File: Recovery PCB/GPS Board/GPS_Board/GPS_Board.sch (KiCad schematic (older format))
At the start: 10 parts, among them J1 XT30-M, J2 XT30-M, U1 Teensy4.1

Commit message: Added regulator symbols
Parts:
- removed A3: Eboot-MP1584EN-5V-Power-Supply, GPS Board:EBOOT-MP1584EN-5N-POWER-SUPPLY, symbol eboot-mp1584en-5v-power-supply:Eboot-MP1584EN-5V-Power-Supply
- added U?: D24V22F5_VoltageRegulator, symbol GPS_Board:D24V22F5_VoltageRegulator
- added U?: LD1117v33, symbol GPS_Board:LD1117v33
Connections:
- wire segments 52 -> 53
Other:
- moved on the sheet: J1, J2
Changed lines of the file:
@@
-$EndComp
-$Comp
-L eboot-mp1584en-5v-power-supply:Eboot-MP1584EN-5V-Power-Supply A3
-U 1 1 61A8FD6D
-P 9400 1950
-F 0 "A3" H 9400 2615 50  0000 C CNN
-F 1 "Eboot-MP1584EN-5V-Power-Supply" H 9400 2524 50  0000 C CNN
-F 2 "GPS Board:EBOOT-MP1584EN-5N-POWER-SUPPLY" H 9400 1950 50  0001 C CNN
-F 3 "" H 9400 1950 50  0001 C CNN
-	1    9400 1950
-	1    0    0    -1
 $EndComp
 $Comp
 L GPS_Board:XT30-M J1
 U 1 1 61A95F1A
-P 7250 2000
-F 0 "J1" V 7216 2468 50  0000 L CNN
-F 1 "XT30-M" V 7307 2468 50  0000 L CNN
-F 2 "Connector_AMASS:AMASS_XT30U-M_1x02_P5.0mm_Vertical" H 7250 2000 50  0001 C CNN
-F 3 "" H 7250 2000 50  0001 C CNN
-	1    7250 2000
+P 7225 1400
+F 0 "J1" V 7191 1868 50  0000 L CNN
+F 1 "XT30-M" V 7282 1868 50  0000 L CNN
+F 2 "Connector_AMASS:AMASS_XT30U-M_1x02_P5.0mm_Vertical" H 7225 1400 50  0001 C CNN
+F 3 "" H 7225 1400 50  0001 C CNN
+	1    7225 1400
 	0    1    1    0
 $EndComp
@@
 L GPS_Board:XT30-M J2
 U 1 1 61A98361
-P 8100 2300
-F 0 "J2" H 7923 2466 50  0000 R CNN
-F 1 "XT30-M" H 7923 2557 50  0000 R CNN
-F 2 "Connector_AMASS:AMASS_XT30U-M_1x02_P5.0mm_Vertical" H 8100 2300 50  0001 C CNN
-F 3 "" H 8100 2300 50  0001 C CNN
-	1    8100 2300
+P 8075 1700
+F 0 "J2" H 7898 1866 50  0000 R CNN
+F 1 "XT30-M" H 7898 1957 50  0000 R CNN
+F 2 "Connector_AMASS:AMASS_XT30U-M_1x02_P5.0mm_Vertical" H 8075 1700 50  0001 C CNN
+F 3 "" H 8075 1700 50  0001 C CNN
+	1    8075 1700
 	-1   0    0    1
 $EndComp
 Wire Wire Line
-	7250 2100 7100 2100
-Wire Wire Line
-	7100 2100 7100 2250
-Wire Wire Line
-	7100 2250 8000 2250
-Wire Wire Line
-	8000 2250 8000 2300
-Wire Wire Line
-	8175 2300 8175 2250
-Wire Wire Line
-	8175 2250 8600 2250
-Wire Wire Line
-	8600 2250 8600 2400
-Wire Wire Line
-	8600 1550 7075 1550
-Wire Wire Line
-	7075 1550 7075 1925
-Wire Wire Line
-	7075 1925 7250 1925
+	7225 1500 7075 1500
+Wire Wire Line
+	7075 1500 7075 1650
+Wire Wire Line
+	7075 1650 7975 1650
+Wire Wire Line
+	7975 1650 7975 1700
+Wire Wire Line
+	8150 1700 8150 1650
+Wire Wire Line
+	8150 1650 8575 1650
+Wire Wire Line
+	8575 1650 8575 1800
+Wire Wire Line
+	6975 1325 7225 1325
 $Comp
 L GPS_Board:Sparkfun-GPS-Breakout A2
@@
 F 3 "" H 4000 1500 50  0001 C CNN
 	1    4000 1500
-	0    -1   -1   0
-$EndComp
-$Comp
-L power:GND #PWR0104
-U 1 1 61AC16D1
-P 10200 1550
-F 0 "#PWR0104" H 10200 1300 50  0001 C CNN
-F 1 "GND" V 10205 1422 50  0000 R CNN
-F 2 "" H 10200 1550 50  0001 C CNN
-F 3 "" H 10200 1550 50  0001 C CNN
-	1    10200 1550
 	0    -1   -1   0
 $EndComp
@@
 	0    1    1    0
 $EndComp
-$Comp
-L power:+5V #PWR0108
-U 1 1 61AD2A6D
-P 10200 2400
-F 0 "#PWR0108" H 10200 2250 50  0001 C CNN
-F 1 "+5V" V 10215 2528 50  0000 L CNN
-F 2 "" H 10200 2400 50  0001 C CNN
-F 3 "" H 10200 2400 50  0001 C CNN
-	1    10200 2400
-	0    1    1    0
-$EndComp
 Wire Wire Line
 	2900 4850 2950 4850
@@
 	1    0    0    -1
 $EndComp
-$Comp
-L power:GND #PWR?
-U 1 1 61BA5EBA
-P 7075 1550
-F 0 "#PWR?" H 7075 1300 50  0001 C CNN
-F 1 "GND" H 7080 1377 50  0000 C CNN
-F 2 "" H 7075 1550 50  0001 C CNN
-F 3 "" H 7075 1550 50  0001 C CNN
-	1    7075 1550
-	-1   0    0    1
-$EndComp
-Connection ~ 7075 1550
 Wire Wire Line
 	4000 2200 4300 2200
@@
 Text Label 4400 3200 2    39   ~ 0
 XBee_DTR
-Text Label 6675 1925 2    39   ~ 0
-ON_SLEEP
 Wire Wire Line
 	4000 3700 4425 3700
@@
 Wire Wire Line
 	6275 1525 6575 1525
-Wire Wire Line
-	6275 1925 6675 1925
 Wire Wire Line
 	6275 2125 6675 2125
@@
 Text Label 4300 2400 2    39   ~ 0
 XBEE_SCL
+Wire Wire Line
+	6275 1925 6675 1925
+Text Label 6675 1925 2    39   ~ 0
+ON_SLEEP
+$Comp
+L GPS_Board:D24V22F5_VoltageRegulator U?
+U 1 1 6257FB96
+P 9300 1900
+F 0 "U?" H 9578 1946 50  0000 L CNN
+F 1 "D24V22F5_VoltageRegulator" H 9578 1855 50  0000 L CNN
+F 2 "" H 9750 3100 50  0001 C CNN
+F 3 "" H 9750 3100 50  0001 C CNN
+	1    9300 1900
+	1    0    0    -1
+$EndComp
+Wire Wire Line
+	8950 1800 8575 1800
+$Comp
+L power:GND #PWR?
+U 1 1 62587171
+P 6975 1325
+F 0 "#PWR?" H 6975 1075 50  0001 C CNN
+F 1 "GND" H 6980 1152 50  0000 C CNN
+F 2 "" H 6975 1325 50  0001 C CNN
+F 3 "" H 6975 1325 50  0001 C CNN
+	1    6975 1325
+	1    0    0    -1
+$EndComp
+$Comp
+L power:+5V #PWR?
+U 1 1 62588B60
+P 8950 2100
+F 0 "#PWR?" H 8950 1950 50  0001 C CNN
+F 1 "+5V" V 8965 2228 50  0000 L CNN
+F 2 "" H 8950 2100 50  0001 C CNN
+F 3 "" H 8950 2100 50  0001 C CNN
+	1    8950 2100
+	0    -1   -1   0
+$EndComp
+$Comp
+L power:GND #PWR?
+U 1 1 62589874
+P 8950 1900
+F 0 "#PWR?" H 8950 1650 50  0001 C CNN
+F 1 "GND" V 8955 1772 50  0000 R CNN
+F 2 "" H 8950 1900 50  0001 C CNN
+F 3 "" H 8950 1900 50  0001 C CNN
+	1    8950 1900
+	0    1    1    0
+$EndComp
+$Comp
+L power:GND #PWR?
+U 1 1 6258A3E2
+P 8950 2000
+F 0 "#PWR?" H 8950 1750 50  0001 C CNN
+F 1 "GND" V 8955 1872 50  0000 R CNN
+F 2 "" H 8950 2000 50  0001 C CNN
+F 3 "" H 8950 2000 50  0001 C CNN
+	1    8950 2000
+	0    1    1    0
+$EndComp
+$Comp
+L GPS_Board:LD1117v33 U?
+U 1 1 625AB452
+P 9300 2675
+F 0 "U?" H 9290 3020 50  0000 C CNN
+F 1 "LD1117v33" H 9290 2929 50  0000 C CNN
+F 2 "" H 9290 2905 50  0001 C CNN
+F 3 "" H 9290 2905 50  0001 C CNN
+	1    9300 2675
+	1    0    0    -1
+$EndComp
+Wire Wire Line
+	8575 2675 8575 1800
+Connection ~ 8575 1800
+Wire Wire Line
+	8575 2675 8940 2675
+$Comp
+L power:GND #PWR?
+U 1 1 625C6B48
+P 9640 2765
+F 0 "#PWR?" H 9640 2515 50  0001 C CNN
+F 1 "GND" V 9645 2637 50  0000 R CNN
+F 2 "" H 9640 2765 50  0001 C CNN
+F 3 "" H 9640 2765 50  0001 C CNN
+	1    9640 2765
+	0    -1   -1   0
+$EndComp
+$Comp
+L power:+3.3V #PWR?
+U 1 1 625C7E59
+P 9640 2605
+F 0 "#PWR?" H 9640 2455 50  0001 C CNN
+F 1 "+3.3V" V 9655 2733 50  0000 L CNN
+F 2 "" H 9640 2605 50  0001 C CNN
+F 3 "" H 9640 2605 50  0001 C CNN
+	1    9640 2605
+	0    1    1    0
+$EndComp
 $EndSCHEMATC

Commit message: Added footprint to 3.3v regulator
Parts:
- U?: footprint (none) -> GPS Board:D24V22F5_VoltageRegulator
- U?: footprint (none) -> Package_TO_SOT_THT:TO-220-3_Horizontal_TabDown
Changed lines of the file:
@@
 F 0 "U?" H 9578 1946 50  0000 L CNN
 F 1 "D24V22F5_VoltageRegulator" H 9578 1855 50  0000 L CNN
-F 2 "" H 9750 3100 50  0001 C CNN
+F 2 "GPS Board:D24V22F5_VoltageRegulator" H 9750 3100 50  0001 C CNN
 F 3 "" H 9750 3100 50  0001 C CNN
 	1    9300 1900
@@
 F 0 "U?" H 9290 3020 50  0000 C CNN
 F 1 "LD1117v33" H 9290 2929 50  0000 C CNN
-F 2 "" H 9290 2905 50  0001 C CNN
+F 2 "Package_TO_SOT_THT:TO-220-3_Horizontal_TabDown" H 9290 2905 50  0001 C CNN
 F 3 "" H 9290 2905 50  0001 C CNN
 	1    9300 2675

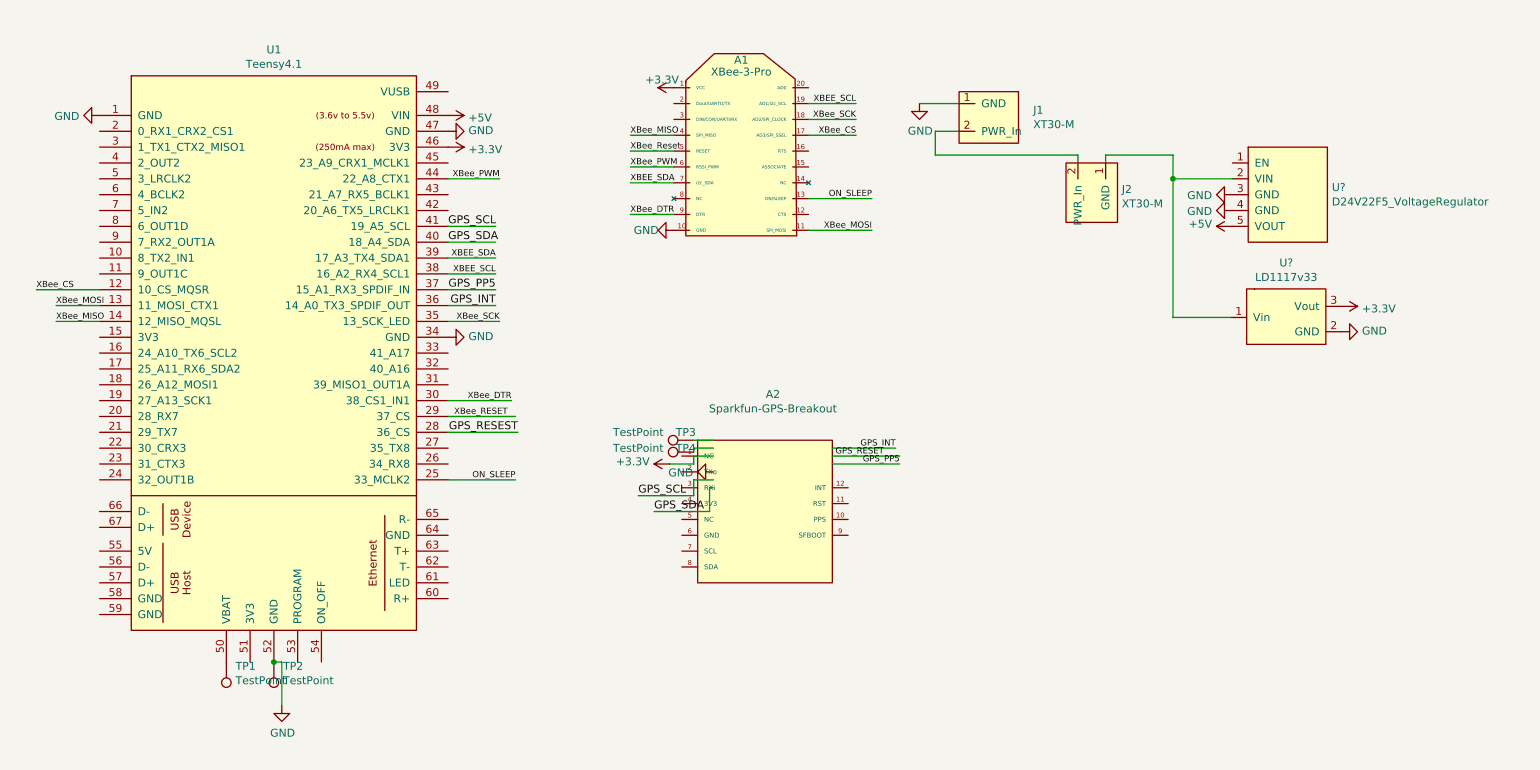
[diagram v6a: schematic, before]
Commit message: Added UART labels and testpoints
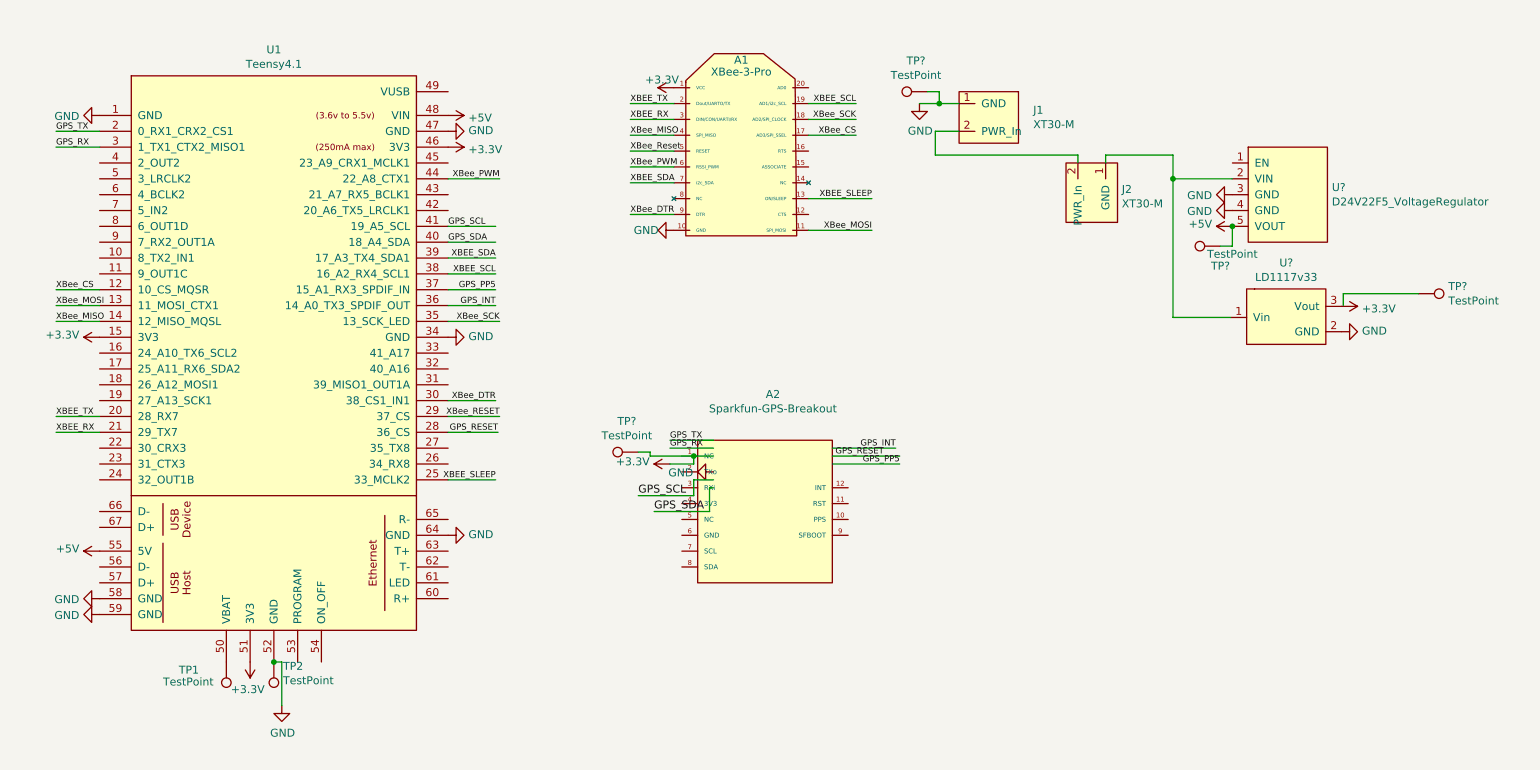
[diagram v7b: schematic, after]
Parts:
- removed TP3, TP4: TestPoint, TestPoint:TestPoint_Pad_D1.5mm, symbol Connector:TestPoint
- added TP? (x4): TestPoint, symbol Connector:TestPoint
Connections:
- net labels added: GPS_RX, GPS_TX, XBEE_RX, XBEE_SLEEP, XBEE_TX
- net labels removed: GPS_RESEST, ON_SLEEP
- wire segments 53 -> 68
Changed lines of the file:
@@
 	8575 1650 8575 1800
 Wire Wire Line
-	6975 1325 7225 1325
+	6975 1325 7100 1325
 $Comp
 L GPS_Board:Sparkfun-GPS-Breakout A2
@@
 	1    0    0    -1
 $EndComp
-$Comp
-L Connector:TestPoint TP3
-U 1 1 61AB8223
-P 5550 3450
-F 0 "TP3" V 5600 3500 50  0000 C CNN
-F 1 "TestPoint" V 5600 3800 50  0000 C CNN
-F 2 "TestPoint:TestPoint_Pad_D1.5mm" H 5750 3450 50  0001 C CNN
-F 3 "~" H 5750 3450 50  0001 C CNN
-	1    5550 3450
-	0    -1   -1   0
-$EndComp
-$Comp
-L Connector:TestPoint TP4
-U 1 1 61AB9396
-P 5550 3525
-F 0 "TP4" V 5575 3575 50  0000 C CNN
-F 1 "TestPoint" V 5575 3875 50  0000 C CNN
-F 2 "TestPoint:TestPoint_Pad_D1.5mm" H 5750 3525 50  0001 C CNN
-F 3 "~" H 5750 3525 50  0001 C CNN
-	1    5550 3525
-	0    -1   -1   0
-$EndComp
-Wire Wire Line
-	5550 3450 5675 3450
-Wire Wire Line
-	5550 3525 5550 3500
-Wire Wire Line
-	5550 3500 5675 3500
+Wire Wire Line
+	5400 3450 5675 3450
+Wire Wire Line
+	5400 3500 5675 3500
 $Comp
 L power:GND #PWR0101
@@
 U 1 1 61ACF9DD
 P 2600 4850
-F 0 "TP1" H 2542 4876 50  0000 R CNN
-F 1 "TestPoint" H 2542 4967 50  0000 R CNN
+F 0 "TP1" H 2900 4900 50  0000 R CNN
+F 1 "TestPoint" H 3000 4975 50  0000 R CNN
 F 2 "TestPoint:TestPoint_Pad_D1.5mm" H 2800 4850 50  0001 C CNN
 F 3 "~" H 2800 4850 50  0001 C CNN
@@
 Wire Wire Line
 	5650 3750 5675 3750
-Text Label 4000 2100 0    50   ~ 0
+Text Label 4000 2100 0    39   ~ 0
 GPS_SCL
-Text Label 4000 2200 0    50   ~ 0
+Text Label 4000 2200 0    39   ~ 0
 GPS_SDA
 Text Label 5200 3800 0    50   ~ 0
@@
 	0    -1   -1   0
 $EndComp
-Text Label 4440 3400 2    50   ~ 0
-GPS_RESEST
-Wire Wire Line
-	4000 3400 4440 3400
+Text Label 4315 3400 2    39   ~ 0
+GPS_RESET
+Wire Wire Line
+	4000 3400 4315 3400
 Text Label 6750 3550 2    39   ~ 0
 GPS_RESET
@@
 Wire Wire Line
 	6425 3600 6850 3600
-Text Label 4300 2500 2    50   ~ 0
+Text Label 4300 2500 2    39   ~ 0
 GPS_PP5
 Wire Wire Line
@@
 Wire Wire Line
 	4000 2600 4300 2600
-Text Label 4300 2600 2    50   ~ 0
+Text Label 4300 2600 2    39   ~ 0
 GPS_INT
 Text Label 6825 3500 2    39   ~ 0
@@
 Text Label 6575 1425 2    39   ~ 0
 XBee_SCK
-Text Label 1400 2500 0    39   ~ 0
+Text Label 1525 2500 0    39   ~ 0
 XBee_CS
 Wire Wire Line
-	1400 2500 1800 2500
+	1525 2500 1800 2500
 $Comp
 L power:+3.3V #PWR?
@@
 	1800 2700 1525 2700
 Wire Wire Line
-	4000 3300 4425 3300
-Text Label 4375 3300 2    39   ~ 0
+	4000 3300 4325 3300
+Text Label 4325 3300 2    39   ~ 0
 XBee_RESET
 Text Label 5150 1725 0    39   ~ 0
@@
 XBee_DTR
 Wire Wire Line
-	4000 3200 4400 3200
-Text Label 4400 3200 2    39   ~ 0
+	4000 3200 4300 3200
+Text Label 4300 3200 2    39   ~ 0
 XBee_DTR
 Wire Wire Line
-	4000 3700 4425 3700
-Text Label 4425 3700 2    39   ~ 0
-ON_SLEEP
+	4000 3700 4300 3700
+Text Label 4300 3700 2    39   ~ 0
+XBEE_SLEEP
 $Comp
 L power:+3.3V #PWR?
@@
 Text Label 6675 2125 2    39   ~ 0
 XBee_MOSI
-Wire Wire Line
-	6275 1525 6575 1525
-Wire Wire Line
-	6275 2125 6675 2125
 Wire Wire Line
 	5425 2025 5150 2025
@@
 	5150 1525 5425 1525
 Wire Wire Line
-	6275 1425 6575 1425
-Wire Wire Line
 	5150 1825 5425 1825
-Wire Wire Line
-	6275 1325 6575 1325
 Text Label 5150 1825 0    39   ~ 0
 XBEE_SDA
@@
 Text Label 4300 2400 2    39   ~ 0
 XBEE_SCL
-Wire Wire Line
-	6275 1925 6675 1925
 Text Label 6675 1925 2    39   ~ 0
-ON_SLEEP
+XBEE_SLEEP
 $Comp
 L GPS_Board:D24V22F5_VoltageRegulator U?
@@
 	0    1    1    0
 $EndComp
+Wire Wire Line
+	1800 3300 1525 3300
+Wire Wire Line
+	1800 3400 1525 3400
+Wire Wire Line
+	6275 1525 6575 1525
+Wire Wire Line
+	6275 2125 6675 2125
+Wire Wire Line
+	6275 1425 6575 1425
+Wire Wire Line
+	6275 1325 6575 1325
+Wire Wire Line
+	6275 1925 6675 1925
+Wire Wire Line
+	5425 1325 5150 1325
+Wire Wire Line
+	5425 1425 5150 1425
+Text Label 5150 1325 0    39   ~ 0
+XBEE_TX
+Text Label 5150 1425 0    39   ~ 0
+XBEE_RX
+Text Label 1525 3300 0    39   ~ 0
+XBEE_TX
+Text Label 1525 3400 0    39   ~ 0
+XBEE_RX
+Text Label 5400 3450 0    39   ~ 0
+GPS_TX
+Text Label 5400 3500 0    39   ~ 0
+GPS_RX
+Wire Wire Line
+	1800 1500 1525 1500
+Wire Wire Line
+	1800 1600 1525 1600
+Text Label 1525 1500 0    39   ~ 0
+GPS_TX
+Text Label 1525 1600 0    39   ~ 0
+GPS_RX
+$Comp
+L power:+3.3V #PWR?
+U 1 1 625EA16C
+P 2750 4850
+F 0 "#PWR?" H 2750 4700 50  0001 C CNN
+F 1 "+3.3V" H 2765 5023 50  0000 C CNN
+F 2 "" H 2750 4850 50  0001 C CNN
+F 3 "" H 2750 4850 50  0001 C CNN
+	1    2750 4850
+	-1   0    0    1
+$EndComp
+$Comp
+L power:GND #PWR?
+U 1 1 625EB8C1
+P 1800 4550
+F 0 "#PWR?" H 1800 4300 50  0001 C CNN
+F 1 "GND" V 1805 4422 50  0000 R CNN
+F 2 "" H 1800 4550 50  0001 C CNN
+F 3 "" H 1800 4550 50  0001 C CNN
+	1    1800 4550
+	0    1    1    0
+$EndComp
+$Comp
+L power:GND #PWR?
+U 1 1 625EC4CE
+P 1800 4450
+F 0 "#PWR?" H 1800 4200 50  0001 C CNN
+F 1 "GND" V 1805 4322 50  0000 R CNN
+F 2 "" H 1800 4450 50  0001 C CNN
+F 3 "" H 1800 4450 50  0001 C CNN
+	1    1800 4450
+	0    1    1    0
+$EndComp
+$Comp
+L power:+5V #PWR?
+U 1 1 625ECDBB
+P 1800 4150
+F 0 "#PWR?" H 1800 4000 50  0001 C CNN
+F 1 "+5V" V 1815 4278 50  0000 L CNN
+F 2 "" H 1800 4150 50  0001 C CNN
+F 3 "" H 1800 4150 50  0001 C CNN
+	1    1800 4150
+	0    -1   -1   0
+$EndComp
+$Comp
+L power:+3.3V #PWR?
+U 1 1 625EDBA6
+P 1800 2800
+F 0 "#PWR?" H 1800 2650 50  0001 C CNN
+F 1 "+3.3V" V 1815 2928 50  0000 L CNN
+F 2 "" H 1800 2800 50  0001 C CNN
+F 3 "" H 1800 2800 50  0001 C CNN
+	1    1800 2800
+	0    -1   -1   0
+$EndComp
+$Comp
+L power:GND #PWR?
+U 1 1 625EF2C8
+P 4000 4050
+F 0 "#PWR?" H 4000 3800 50  0001 C CNN
+F 1 "GND" V 4005 3922 50  0000 R CNN
+F 2 "" H 4000 4050 50  0001 C CNN
+F 3 "" H 4000 4050 50  0001 C CNN
+	1    4000 4050
+	0    -1   -1   0
+$EndComp
+Wire Wire Line
+	5550 3550 5275 3550
+Wire Wire Line
+	5275 3550 5275 3525
+Wire Wire Line
+	5275 3525 5200 3525
+Connection ~ 5550 3550
+$Comp
+L Connector:TestPoint TP?
+U 1 1 625F3DB9
+P 5200 3525
+F 0 "TP?" V 5395 3597 50  0000 C CNN
+F 1 "TestPoint" V 5304 3597 50  0000 C CNN
+F 2 "" H 5400 3525 50  0001 C CNN
+F 3 "~" H 5400 3525 50  0001 C CNN
+	1    5200 3525
+	0    -1   -1   0
+$EndComp
+Wire Wire Line
+	9650 2600 9650 2525
+Wire Wire Line
+	9650 2525 10125 2525
+$Comp
+L Connector:TestPoint TP?
+U 1 1 625F9755
+P 10125 2525
+F 0 "TP?" V 10079 2713 50  0000 L CNN
+F 1 "TestPoint" V 10170 2713 50  0000 L CNN
+F 2 "" H 10325 2525 50  0001 C CNN
+F 3 "~" H 10325 2525 50  0001 C CNN
+	1    10125 2525
+	0    1    1    0
+$EndComp
+Wire Wire Line
+	8950 2100 8950 2225
+Wire Wire Line
+	8950 2225 8875 2225
+Connection ~ 8950 2100
+$Comp
+L Connector:TestPoint TP?
+U 1 1 625FCCAB
+P 8875 2225
+F 0 "TP?" V 8750 2225 50  0000 C CNN
+F 1 "TestPoint" V 8825 2150 50  0000 C CNN
+F 2 "" H 9075 2225 50  0001 C CNN
+F 3 "~" H 9075 2225 50  0001 C CNN
+	1    8875 2225
+	0    -1   -1   0
+$EndComp
+Wire Wire Line
+	7100 1325 7100 1250
+Wire Wire Line
+	7100 1250 7025 1250
+Connection ~ 7100 1325
+Wire Wire Line
+	7100 1325 7225 1325
+$Comp
+L Connector:TestPoint TP?
+U 1 1 62600FE9
+P 7025 1250
+F 0 "TP?" V 7220 1322 50  0000 C CNN
+F 1 "TestPoint" V 7129 1322 50  0000 C CNN
+F 2 "" H 7225 1250 50  0001 C CNN
+F 3 "~" H 7225 1250 50  0001 C CNN
+	1    7025 1250
+	0    -1   -1   0
+$EndComp
 $EndSCHEMATC
